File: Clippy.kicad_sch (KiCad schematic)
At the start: 15 parts, among them J1 Conn_01x08, SW1 PEC11R-4215F-S0024, U1 tiny2040, U2 SN74LV1T34DBV

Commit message: Final touches?
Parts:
- added C2, C3: 100nF, Capacitor_SMD:C_0402_1005Metric_Pad0.74x0.62mm_HandSolder, symbol Device:C_Small
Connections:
- net +5V: now also C2.1, C3.1
- net GND: now also C2.2, C3.2
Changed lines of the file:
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@@
   (junction (at 111.125 151.765) (diameter 0) (color 0 0 0 0)
   )
+  (junction (at 115.57 128.905) (diameter 0) (color 0 0 0 0)
+  )
+  (junction (at 103.505 123.825) (diameter 0) (color 0 0 0 0)
+  )
   (junction (at 111.125 136.525) (diameter 0) (color 0 0 0 0)
   )
@@
   )
   (junction (at 176.53 133.985) (diameter 0) (color 0 0 0 0)
+  )
+  (junction (at 106.045 123.825) (diameter 0) (color 0 0 0 0)
   )
   (junction (at 88.9 100.33) (diameter 0) (color 0 0 0 0)
@@
     (stroke (width 0) (type default))
   )
-  (wire (pts (xy 103.505 133.35) (xy 103.505 136.525))
+  (wire (pts (xy 103.505 123.825) (xy 103.505 136.525))
     (stroke (width 0) (type default))
   )
@@
     (stroke (width 0) (type default))
   )
+  (wire (pts (xy 106.045 128.905) (xy 115.57 128.905))
+    (stroke (width 0) (type default))
+  )
   (wire (pts (xy 142.875 93.345) (xy 144.145 93.345))
     (stroke (width 0) (type default))
@@
     (stroke (width 0) (type default))
   )
+  (wire (pts (xy 106.045 123.825) (xy 115.57 123.825))
+    (stroke (width 0) (type default))
+  )
   (wire (pts (xy 162.56 86.36) (xy 162.56 85.09))
     (stroke (width 0) (type default))
@@
     (stroke (width 0) (type default))
   )
+  (wire (pts (xy 115.57 128.905) (xy 120.65 128.905))
+    (stroke (width 0) (type default))
+  )
   (wire (pts (xy 90.805 85.09) (xy 88.9 85.09))
     (stroke (width 0) (type default))
@@
   )
   (wire (pts (xy 133.985 151.765) (xy 156.845 151.765))
+    (stroke (width 0) (type default))
+  )
+  (wire (pts (xy 103.505 123.825) (xy 106.045 123.825))
     (stroke (width 0) (type default))
   )
@@
         (path "/4f2cd10c-3737-4f06-830a-6bec39470d35"
           (reference "D4") (unit 1)
+        )
+      )
+    )
+  )
+  (symbol (lib_id "Device:C_Small") (at 106.045 126.365 0) (unit 1)
+    (in_bom yes) (on_board yes) (dnp no)
+    (property "Reference" "C2" (at 107.95 125.73 0)
+      (effects (font (size 1.27 1.27)) (justify left))
+    )
+    (property "Value" "100nF" (at 107.95 127.635 0)
+      (effects (font (size 1.27 1.27)) (justify left))
+    )
+    (property "Footprint" "Capacitor_SMD:C_0402_1005Metric_Pad0.74x0.62mm_HandSolder" (at 106.045 126.365 0)
+      (effects (font (size 1.27 1.27)) hide)
+    )
+    (property "Datasheet" "~" (at 106.045 126.365 0)
+      (effects (font (size 1.27 1.27)) hide)
+    )
+    (property "LCSC" "C1525" (at 106.045 126.365 0)
+      (effects (font (size 1.27 1.27)) hide)
+    )
+    (pin "1")
+    (pin "2")
+    (instances
+      (project "Clippy"
+        (path "/4f2cd10c-3737-4f06-830a-6bec39470d35"
+          (reference "C2") (unit 1)
+        )
+      )
+      (project "PicoLX"
+        (path "/c5e5d8b8-bebd-4318-85a6-adbafb95dd10"
+          (reference "C17") (unit 1)
         )
       )
@@
         (path "/4f2cd10c-3737-4f06-830a-6bec39470d35"
           (reference "J1") (unit 1)
+        )
+      )
+    )
+  )
+  (symbol (lib_id "power:GND") (at 120.65 128.905 0) (unit 1)
+    (in_bom yes) (on_board yes) (dnp no)
+    (property "Reference" "#PWR012" (at 120.65 135.255 0)
+      (effects (font (size 1.27 1.27)) hide)
+    )
+    (property "Value" "GND" (at 120.65 132.715 0)
+      (effects (font (size 1.27 1.27)))
+    )
+    (property "Footprint" "" (at 120.65 128.905 0)
+      (effects (font (size 1.27 1.27)) hide)
+    )
+    (property "Datasheet" "" (at 120.65 128.905 0)
+      (effects (font (size 1.27 1.27)) hide)
+    )
+    (pin "1")
+    (instances
+      (project "Clippy"
+        (path "/4f2cd10c-3737-4f06-830a-6bec39470d35"
+          (reference "#PWR012") (unit 1)
         )
       )
@@
     )
   )
-  (symbol (lib_id "power:+5V") (at 103.505 133.35 0) (unit 1)
-    (in_bom yes) (on_board yes) (dnp no)
-    (property "Reference" "#PWR01" (at 103.505 137.16 0)
-      (effects (font (size 1.27 1.27)) hide)
-    )
-    (property "Value" "+5V" (at 103.505 129.54 0)
-      (effects (font (size 1.27 1.27)))
-    )
-    (property "Footprint" "" (at 103.505 133.35 0)
-      (effects (font (size 1.27 1.27)) hide)
-    )
-    (property "Datasheet" "" (at 103.505 133.35 0)
+  (symbol (lib_id "power:+5V") (at 103.505 123.825 0) (unit 1)
+    (in_bom yes) (on_board yes) (dnp no)
+    (property "Reference" "#PWR01" (at 103.505 127.635 0)
+      (effects (font (size 1.27 1.27)) hide)
+    )
+    (property "Value" "+5V" (at 103.505 120.015 0)
+      (effects (font (size 1.27 1.27)))
+    )
+    (property "Footprint" "" (at 103.505 123.825 0)
+      (effects (font (size 1.27 1.27)) hide)
+    )
+    (property "Datasheet" "" (at 103.505 123.825 0)
       (effects (font (size 1.27 1.27)) hide)
     )
@@
         )
       )
+    )
+  )
+  (symbol (lib_id "Device:C_Small") (at 115.57 126.365 0) (unit 1)
+    (in_bom yes) (on_board yes) (dnp no)
+    (property "Reference" "C3" (at 117.475 125.73 0)
+      (effects (font (size 1.27 1.27)) (justify left))
+    )
+    (property "Value" "100nF" (at 117.475 127.635 0)
+      (effects (font (size 1.27 1.27)) (justify left))
+    )
+    (property "Footprint" "Capacitor_SMD:C_0402_1005Metric_Pad0.74x0.62mm_HandSolder" (at 115.57 126.365 0)
+      (effects (font (size 1.27 1.27)) hide)
+    )
+    (property "Datasheet" "~" (at 115.57 126.365 0)
+      (effects (font (size 1.27 1.27)) hide)
+    )
+    (property "LCSC" "C1525" (at 115.57 126.365 0)
+      (effects (font (size 1.27 1.27)) hide)
+    )
+    (pin "1")
+    (pin "2")
+    (instances
+      (project "Clippy"
+        (path "/4f2cd10c-3737-4f06-830a-6bec39470d35"
+          (reference "C3") (unit 1)
+        )
+      )
+      (project "PicoLX"
+        (path "/c5e5d8b8-bebd-4318-85a6-adbafb95dd10"
+          (reference "C17") (unit 1)
+        )
+      )

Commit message: finishing touches 2 electric boogaloo
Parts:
- C1, C2, C3: footprint Capacitor_SMD:C_0402_1005Metric_Pad0.74x0.62mm_HandSolder -> Capacitor_SMD:C_0805_2012Metric_Pad1.18x1.45mm_HandSolder
- SW1: value PEC11R-4215F-S0024 -> PEC12R-4215F-S0024
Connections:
- net GP7 is gone; now on net GP2: J1.1 (Pin_1)
- net GP2: now reaches U1.14 (GP2)
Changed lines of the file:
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@@
     (stroke (width 0) (type default))
   )
-  (global_label "GP7" (shape input) (at 191.135 78.74 90) (fields_autoplaced)
+  (global_label "GP2" (shape input) (at 191.135 78.74 90) (fields_autoplaced)
     (effects (font (size 1.27 1.27)) (justify left))
     (property "Intersheetrefs" "${INTERSHEET_REFS}" (at 191.135 72.0847 90)
@@
     )
   )
-  (global_label "GP7" (shape input) (at 120.015 66.675 0) (fields_autoplaced)
-    (effects (font (size 1.27 1.27)) (justify left))
-    (property "Intersheetrefs" "${INTERSHEET_REFS}" (at 126.6703 66.675 0)
+  (global_label "GP2" (shape input) (at 114.935 87.63 0) (fields_autoplaced)
+    (effects (font (size 1.27 1.27)) (justify left))
+    (property "Intersheetrefs" "${INTERSHEET_REFS}" (at 121.5903 87.63 0)
       (effects (font (size 1.27 1.27)) (justify left) hide)
     )
@@
       (effects (font (size 1.27 1.27)) (justify left))
     )
-    (property "Footprint" "Capacitor_SMD:C_0402_1005Metric_Pad0.74x0.62mm_HandSolder" (at 106.045 126.365 0)
+    (property "Footprint" "Capacitor_SMD:C_0805_2012Metric_Pad1.18x1.45mm_HandSolder" (at 106.045 126.365 0)
       (effects (font (size 1.27 1.27)) hide)
     )
@@
       (effects (font (size 1.27 1.27)) (justify left))
     )
-    (property "Value" "PEC11R-4215F-S0024" (at 160.02 98.425 90)
+    (property "Value" "PEC12R-4215F-S0024" (at 160.02 98.425 90)
       (effects (font (size 1.27 1.27)) (justify left))
     )
@@
       (effects (font (size 1.27 1.27)))
     )
-    (property "Footprint" "Capacitor_SMD:C_0402_1005Metric_Pad0.74x0.62mm_HandSolder" (at 194.31 121.285 0)
+    (property "Footprint" "Capacitor_SMD:C_0805_2012Metric_Pad1.18x1.45mm_HandSolder" (at 194.31 121.285 0)
       (effects (font (size 1.27 1.27)) hide)
     )
@@
       (effects (font (size 1.27 1.27)) (justify left))
     )
-    (property "Footprint" "Capacitor_SMD:C_0402_1005Metric_Pad0.74x0.62mm_HandSolder" (at 115.57 126.365 0)
-      (effects (font (size 1.27 1.27)) hide)
-    )
+    (property "Footprint" "Capacitor_SMD:C_0805_2012Metric_Pad1.18x1.45mm_HandSolder" (at 115.57 126.365 0)
+      (effects (font (size 1.27 1.27)) hide)
+    )

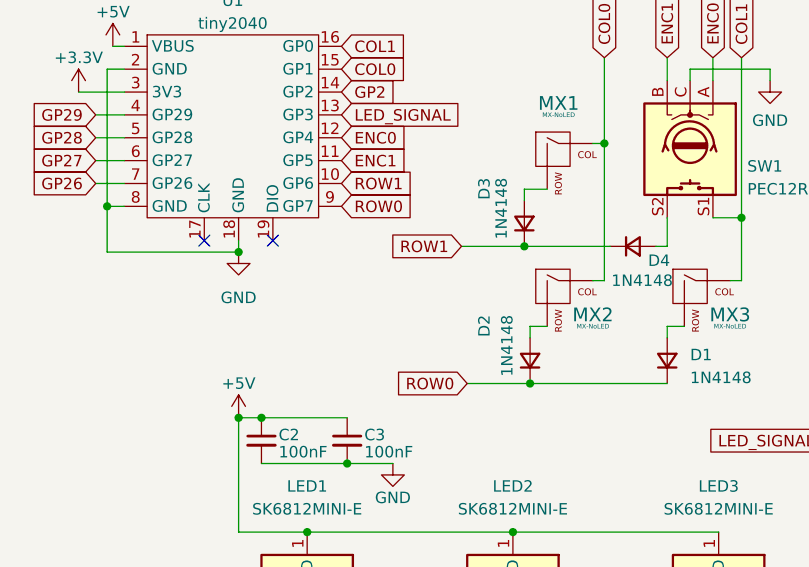
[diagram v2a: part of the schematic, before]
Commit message: oops rows were swapped in the schematic
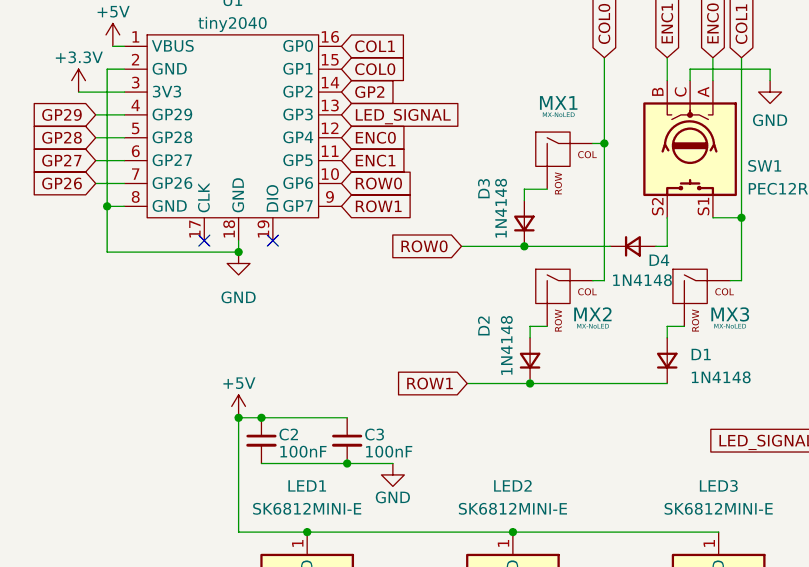
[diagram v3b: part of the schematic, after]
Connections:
- net ROW0: now also D3.1 (K), D4.1 (K), U1.10 (GP6); no longer D1.1 (K), D2.1 (K), U1.9 (GP7)
- net ROW1: now also D1.1 (K), D2.1 (K), U1.9 (GP7); no longer D3.1 (K), D4.1 (K), U1.10 (GP6)
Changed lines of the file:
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@@
     )
   )
-  (global_label "ROW1" (shape input) (at 128.27 104.775 180) (fields_autoplaced)
+  (global_label "ROW0" (shape input) (at 128.27 104.775 180) (fields_autoplaced)
     (effects (font (size 1.27 1.27)) (justify right))
     (property "Intersheetrefs" "${INTERSHEET_REFS}" (at 120.1028 104.775 0)
@@
     )
   )
-  (global_label "ROW1" (shape input) (at 114.935 97.79 0) (fields_autoplaced)
+  (global_label "ROW0" (shape input) (at 114.935 97.79 0) (fields_autoplaced)
     (effects (font (size 1.27 1.27)) (justify left))
     (property "Intersheetrefs" "${INTERSHEET_REFS}" (at 123.1022 97.79 0)
@@
     )
   )
-  (global_label "ROW0" (shape input) (at 114.935 100.33 0) (fields_autoplaced)
+  (global_label "ROW1" (shape input) (at 114.935 100.33 0) (fields_autoplaced)
     (effects (font (size 1.27 1.27)) (justify left))
     (property "Intersheetrefs" "${INTERSHEET_REFS}" (at 123.1022 100.33 0)
@@
     )
   )
-  (global_label "ROW0" (shape input) (at 128.905 120.015 180) (fields_autoplaced)
+  (global_label "ROW1" (shape input) (at 128.905 120.015 180) (fields_autoplaced)
     (effects (font (size 1.27 1.27)) (justify right))
     (property "Intersheetrefs" "${INTERSHEET_REFS}" (at 120.7378 120.015 0)

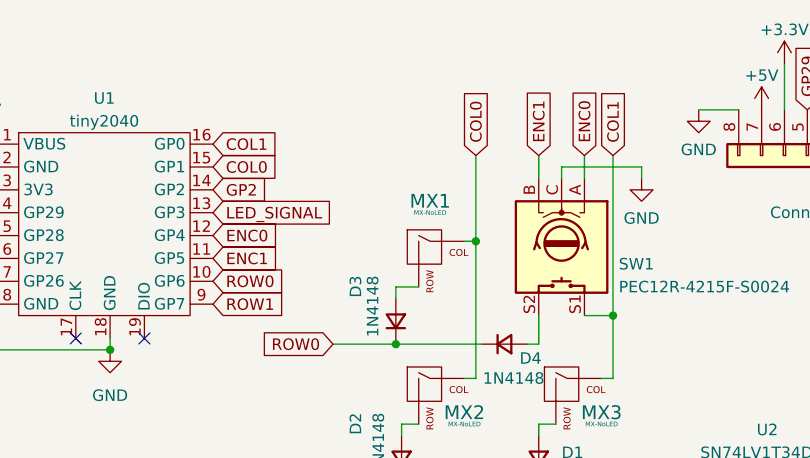
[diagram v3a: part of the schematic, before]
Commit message: Edit schematic labels, initial keymap
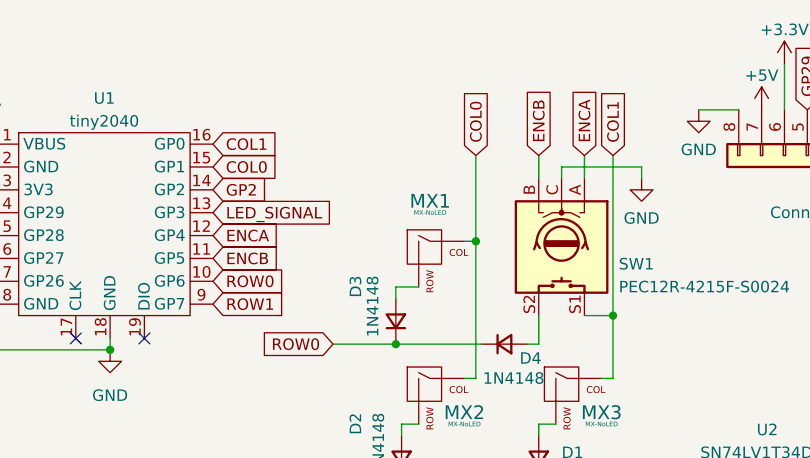
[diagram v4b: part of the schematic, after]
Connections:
- net ENC0 renamed ENCA
- net ENC1 renamed ENCB
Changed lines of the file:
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@@
     )
   )
-  (global_label "ENC1" (shape input) (at 151.13 83.82 90) (fields_autoplaced)
+  (global_label "ENCB" (shape input) (at 151.13 83.82 90) (fields_autoplaced)
     (effects (font (size 1.27 1.27)) (justify left))
-    (property "Intersheetrefs" "${INTERSHEET_REFS}" (at 151.13 75.9552 90)
+    (property "Intersheetrefs" "${INTERSHEET_REFS}" (at 151.13 75.8947 90)
       (effects (font (size 1.27 1.27)) (justify left) hide)
     )
@@
     )
   )
-  (global_label "ENC0" (shape input) (at 114.935 92.71 0) (fields_autoplaced)
+  (global_label "ENCA" (shape input) (at 114.935 92.71 0) (fields_autoplaced)
     (effects (font (size 1.27 1.27)) (justify left))
-    (property "Intersheetrefs" "${INTERSHEET_REFS}" (at 122.7998 92.71 0)
+    (property "Intersheetrefs" "${INTERSHEET_REFS}" (at 122.6789 92.71 0)
       (effects (font (size 1.27 1.27)) (justify left) hide)
     )
@@
     )
   )
-  (global_label "ENC1" (shape input) (at 114.935 95.25 0) (fields_autoplaced)
+  (global_label "ENCB" (shape input) (at 114.935 95.25 0) (fields_autoplaced)
     (effects (font (size 1.27 1.27)) (justify left))
-    (property "Intersheetrefs" "${INTERSHEET_REFS}" (at 122.7998 95.25 0)
+    (property "Intersheetrefs" "${INTERSHEET_REFS}" (at 122.8603 95.25 0)
       (effects (font (size 1.27 1.27)) (justify left) hide)
     )
@@
     )
   )
-  (global_label "ENC0" (shape input) (at 156.21 83.82 90) (fields_autoplaced)
+  (global_label "ENCA" (shape input) (at 156.21 83.82 90) (fields_autoplaced)
     (effects (font (size 1.27 1.27)) (justify left))
-    (property "Intersheetrefs" "${INTERSHEET_REFS}" (at 156.21 75.9552 90)
+    (property "Intersheetrefs" "${INTERSHEET_REFS}" (at 156.21 76.0761 90)
       (effects (font (size 1.27 1.27)) (justify left) hide)
     )

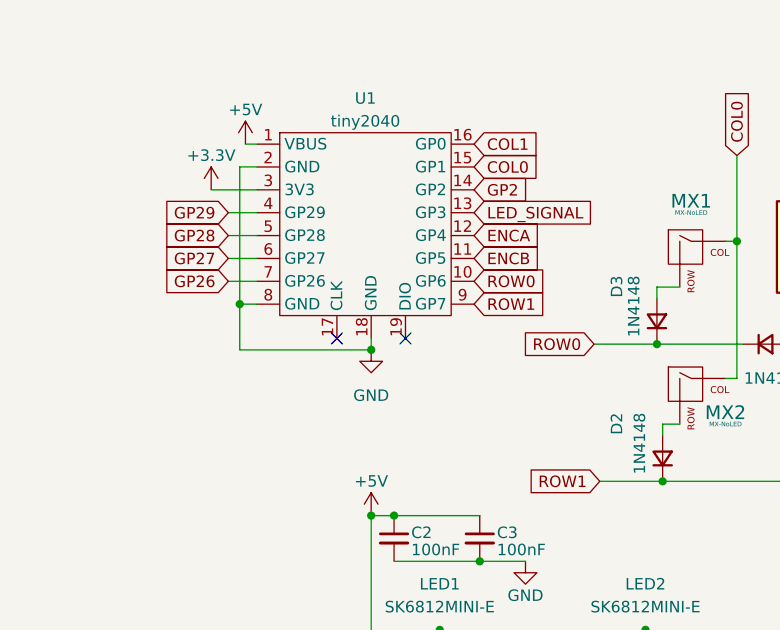
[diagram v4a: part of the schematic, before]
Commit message: RP2040-Zero compatibility
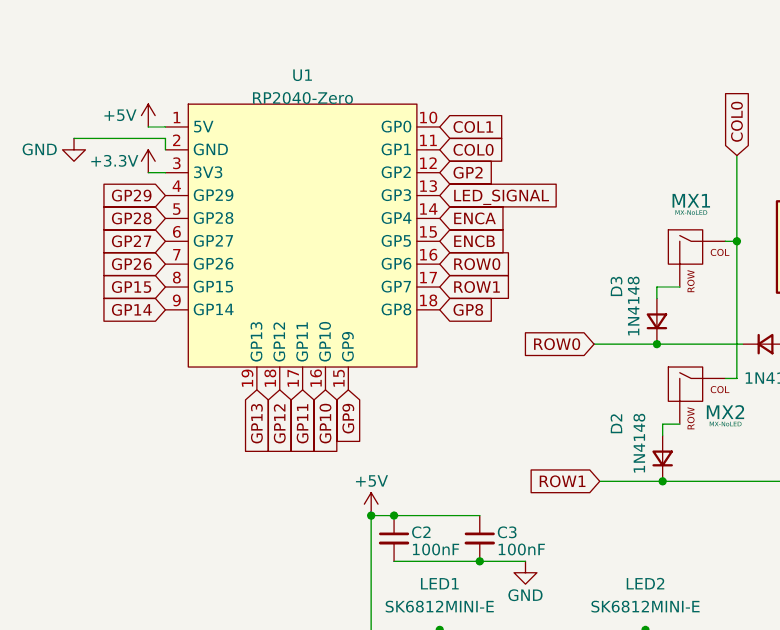
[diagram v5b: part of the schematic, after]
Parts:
- removed U1: tiny2040, tiny2040:tiny2040, symbol tiny2040:tiny2040
- added U1: RP2040-Zero, RP2040-Zero:RP2040 Zero, symbol RP2040-Zero:RP2040-Zero
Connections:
- net +3.3V: now also U1.3 (3V3)
- net +5V: now also U1.1 (5V)
- net COL0: now also U1.11 (GP1)
- net COL1: now also U1.10 (GP0)
- net ENCA: now also U1.14 (GP4)
- net ENCB: now also U1.15 (GP9)
- net GND: now also U1.2 (GND)
- net GP2: now also U1.12 (GP2)
- net GP26: now also U1.7 (GP26)
- net GP27: now also U1.6 (GP27)
- net GP28: now also U1.5 (GP28)
- net GP29: now also U1.4 (GP29)
- net LED_SIGNAL: now also U1.13 (GP3)
- net ROW0: now also U1.16 (GP6)
- net ROW1: now also U1.17 (GP7)
- new net GP10: U1.16 (GP6)
- new net GP11: U1.17 (GP7)
- new net GP12: U1.18 (GP8)
- new net GP13: U1.19 (GP13)
- new net GP14: U1.9 (GP14)
- new net GP15: U1.8 (GP15)
- new net GP8: U1.18 (GP8)
- new net GP9: U1.15 (GP9)
- no-connect marks 3 -> 1
